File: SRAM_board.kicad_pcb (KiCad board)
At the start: 4 copper layers, 108 x 70 mm, 84 parts, among them J1 JP3, J10 Optional Interrupt Pins, J11 Optional Interrupt Pin, J12 GPIO 1, J13 GPIO 0, J14 USB_OTG, J2 JP6, J3 JP2, J4 JP5, J5 Screw_Terminal_01x09, J6 Screw_Terminal_01x06, J7 Optional I2C/UART, J9 Optional Interrupt Pin, SW1 KEY1, SW2 KEY0, U1 LD1085D2T33R, U2 MS561101BA03-50, U3 IIS2MDCTR, U4 GS832032AGT-150I, U5 BMI055, U6 ICM-20689, U7 FT232RL

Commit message: gerbers
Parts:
- moved G*** 2.62 mm to (2.16, -9.86)
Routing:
- net /CLK: track 45.7 -> 81.7 mm
- net /~BW: track 42.7 -> 42.1 mm

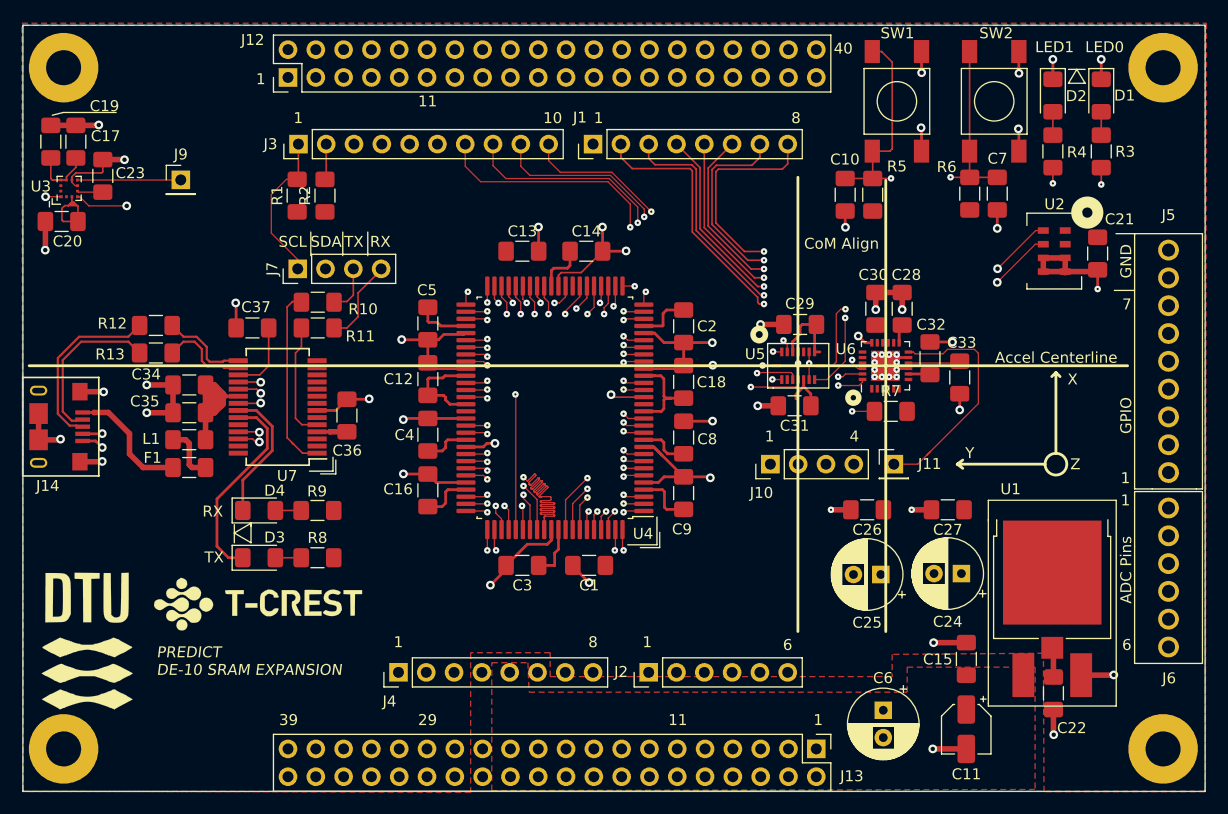
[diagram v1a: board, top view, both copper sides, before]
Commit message: celanup, I2C improvment, SRAM clock buffer
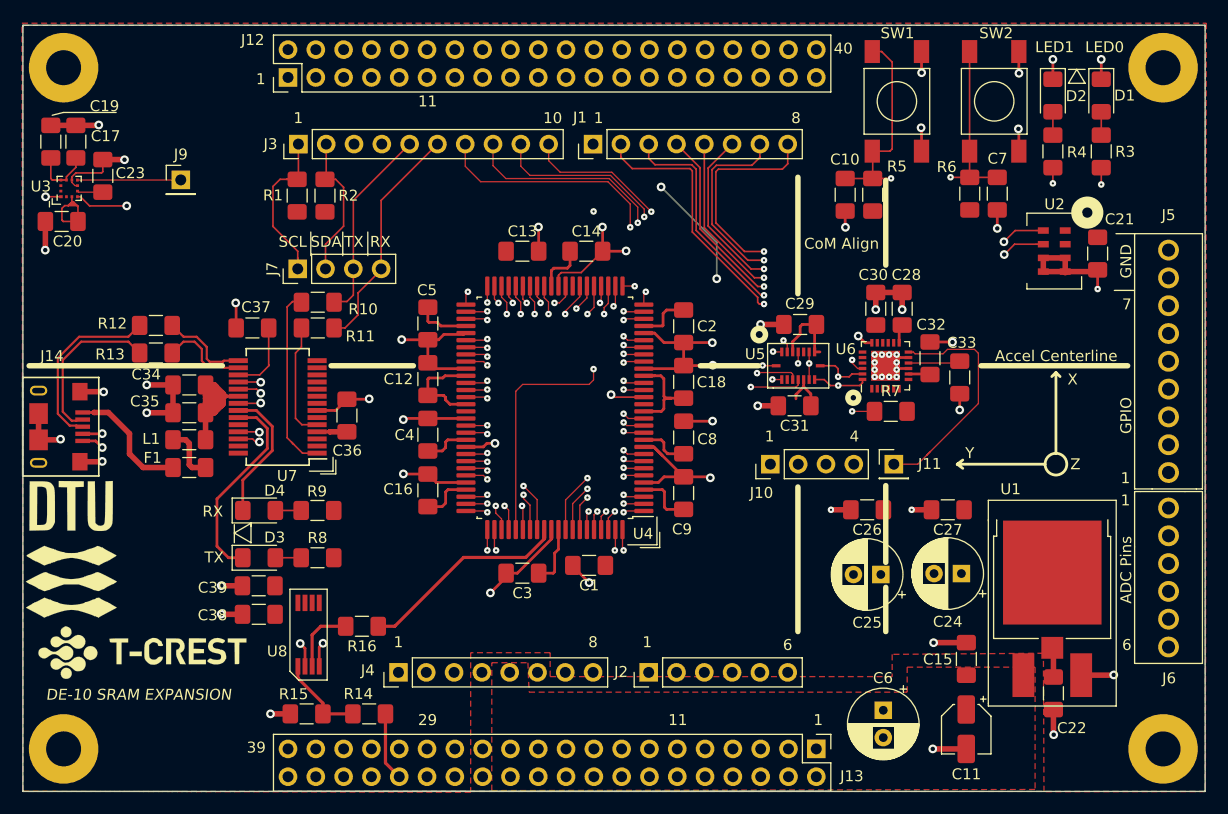
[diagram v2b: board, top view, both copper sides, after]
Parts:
- added C38: 2.2uF, Capacitor_SMD:C_1206_3216Metric_Pad1.42x1.75mm_HandSolder, F.Cu at (17.8, -12.3)
- added C39: 100nF, Capacitor_SMD:C_1206_3216Metric_Pad1.42x1.75mm_HandSolder, F.Cu at (17.8, -14.9)
- added R14: 50R, Resistor_SMD:R_1206_3216Metric_Pad1.42x1.75mm_HandSolder, F.Cu at (27.9, -3.20)
- added R15: 50R, Resistor_SMD:R_1206_3216Metric_Pad1.42x1.75mm_HandSolder, F.Cu at (22.2, -3.20)
- added R16: 50R, Resistor_SMD:R_1206_3216Metric_Pad1.42x1.75mm_HandSolder, F.Cu at (27.3, -11.2)
- added U8: CDCLVC1102, DE10_SRAM_board:SOIC-8, F.Cu at (22.4, -10.4)
- moved G*** 11.5 mm to (7.19, -8.38)
- moved G*** 8.51 mm to (0.71, -18.2)
- moved C3 0.71 mm to (41.9, -16.1)
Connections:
- J13 pad 32: /CLK -> /CLK_IN
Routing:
- net /CLK: track 81.7 -> 19.3 mm, vias 1 -> 0
- net GND: track 198.5 -> 209.0 mm, vias 69 -> 74
- net /I2C_SDA: track 137.7 -> 127.3 mm, vias 4 -> 3
- net Net-(R14-Pad1): track 0.00 -> 8.03 mm
- net Net-(R16-Pad2): track 0.00 -> 6.26 mm
- net /CLK_IN: track 0.00 -> 6.26 mm
- net /I2C_SCL: track 144.4 -> 139.8 mm, vias 4 -> 5
- net /UART_RX: track 35.8 -> 32.5 mm
- net /~ADSC: track 41.1 -> 41.8 mm, vias 1 -> 2
- net +3V3: track 92.3 -> 92.9 mm
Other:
- board text added: "DE-10 SRAM EXPANSION"
- board text removed: "PREDICT DE-10 SRAM EXPANSION"
